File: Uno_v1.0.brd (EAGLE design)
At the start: 68.6 x 53.3 mm, 60 parts, among them CN1 POWER_JACK, CN2 47346-0001, CN3 DIGITAL10, CN4 DIGITAL8, CN5 ICSP, CN6 POWER8, CN7 ANALOG6, IC1 AMS1117-5.0, IC2 AMS1117-3.3, IC3 MCP6002T-I/SN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

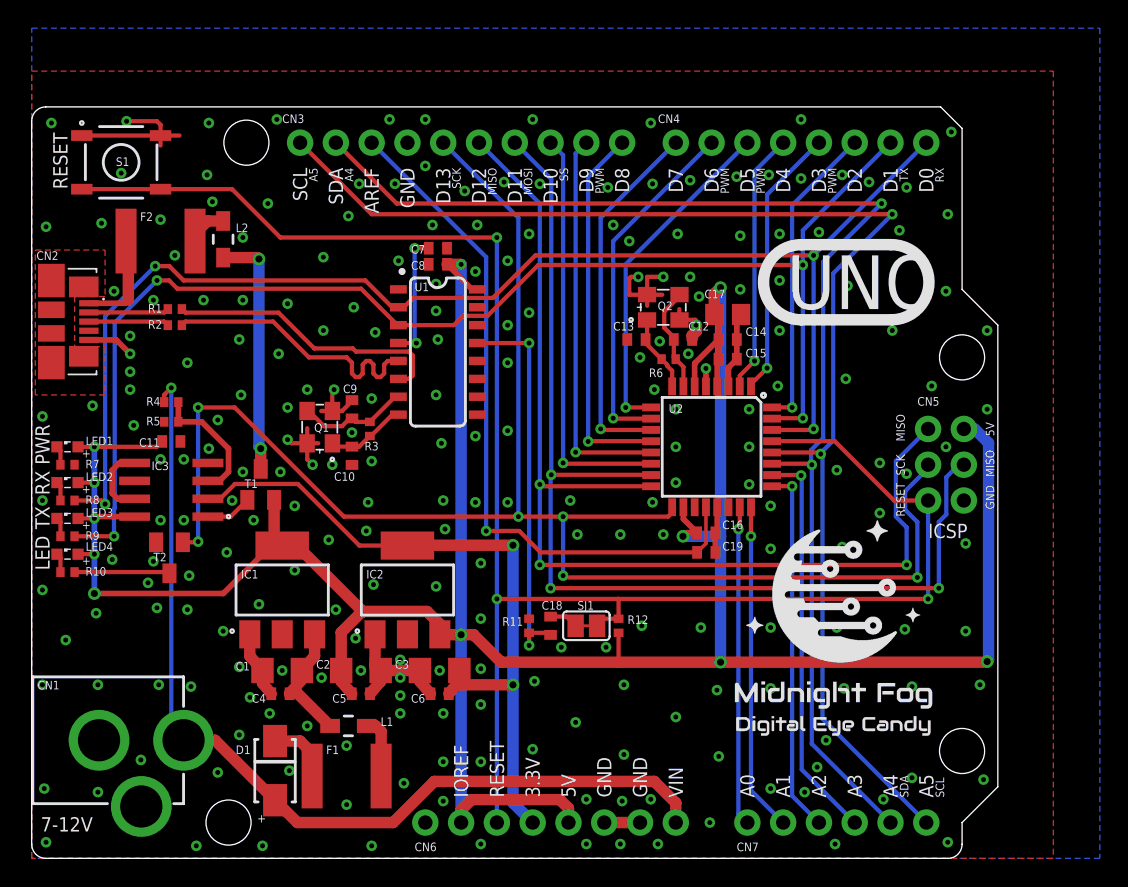
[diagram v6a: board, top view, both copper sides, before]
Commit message: Add second footprint for atmega328. Move components a little.
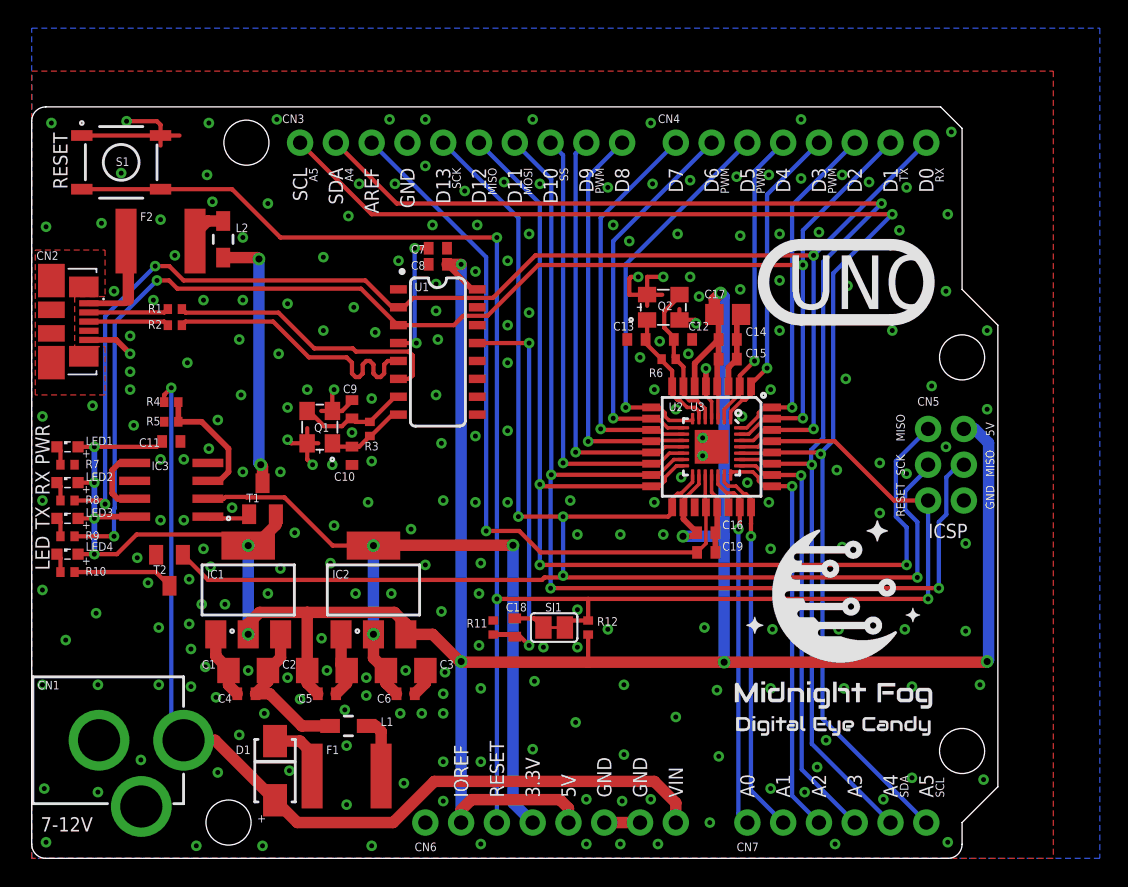
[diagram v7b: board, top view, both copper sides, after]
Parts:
- added U3: ATMEGA328P-MU, SparkFun-IC-Microcontroller:VQFN-28
- moved C18 2.54 mm to (34.3, 16.4)
- moved R11 2.54 mm to (32.8, 16.4)
- moved C1 2.41 mm to (15.4, 13.3)
- moved C2 2.41 mm to (21.0, 13.3)
- moved C3 2.41 mm to (26.5, 13.3), turned to 0 degrees
- moved C5 2.41 mm to (21.0, 11.7)
- moved C6 2.41 mm to (26.5, 11.7), turned to 0 degrees
- moved IC1 2.41 mm to (15.4, 19.1)
- moved IC2 2.41 mm to (24.3, 19.1)
- moved C4 2.41 mm to (15.2, 11.7)
- moved SJ1 2.29 mm to (37.1, 16.4)
- moved R12 2.16 mm to (39.5, 16.4)
- moved T1 1.02 mm to (16.4, 25.5)
- moved T2 0.89 mm to (9.78, 20.4)
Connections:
- net 5V: now also U3.16, U3.3
- net A0: now also U3.19
- net A1: now also U3.20
- net A2: now also U3.21
- net A3: now also U3.22
- net A4_SDA: now also U3.23
- net A5_SCL: now also U3.24
- net AREF: now also U3.17
- net D0_RX: now also U3.26
- net D10_SS: now also U3.12
- net D11_MOSI: now also U3.13
- net D12_MISO: now also U3.14
- net D13_SCK: now also U3.15
- net D1_TX: now also U3.27
- net D2: now also U3.28
- net D3_PWM: now also U3.1
- net D4: now also U3.2
- net D5_PWM: now also U3.7
- net D6_PWM: now also U3.8
- net D7: now also U3.9
- net D8: now also U3.10
- net D9_PWM: now also U3.11
- net GND: now also U3.18, U3.4, U3.PAD
- net MCU_OSC_IN: now also U3.5
- net MCU_OSC_OUT: now also U3.6
- net RESET: now also U3.25
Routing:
- net 5V: track 219.2 -> 225.0 mm, vias 11 -> 12
- net D13_SCK: track 115.2 -> 109.5 mm, vias 6 -> 4
- net 3.3V: track 50.8 -> 55.4 mm, vias 2 -> 3
- net A2: track 26.1 -> 29.8 mm
- net D5_PWM: track 24.2 -> 27.8 mm
- net MCU_OSC_OUT: track 5.54 -> 9.05 mm
- net A1: track 23.3 -> 26.8 mm
- net MCU_OSC_IN: track 7.53 -> 10.8 mm
- net A0: track 22.7 -> 25.9 mm
- net D12_MISO: track 76.7 -> 79.7 mm
- net D3_PWM: track 19.3 -> 22.3 mm
- net D2: track 22.1 -> 25.1 mm
- net D11_MOSI: track 77.1 -> 79.8 mm
- net D4: track 18.6 -> 21.3 mm
- net D1_TX: track 95.5 -> 98.2 mm
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
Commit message: Rotated CH340G 180 degrees. Moved stuff around a little.
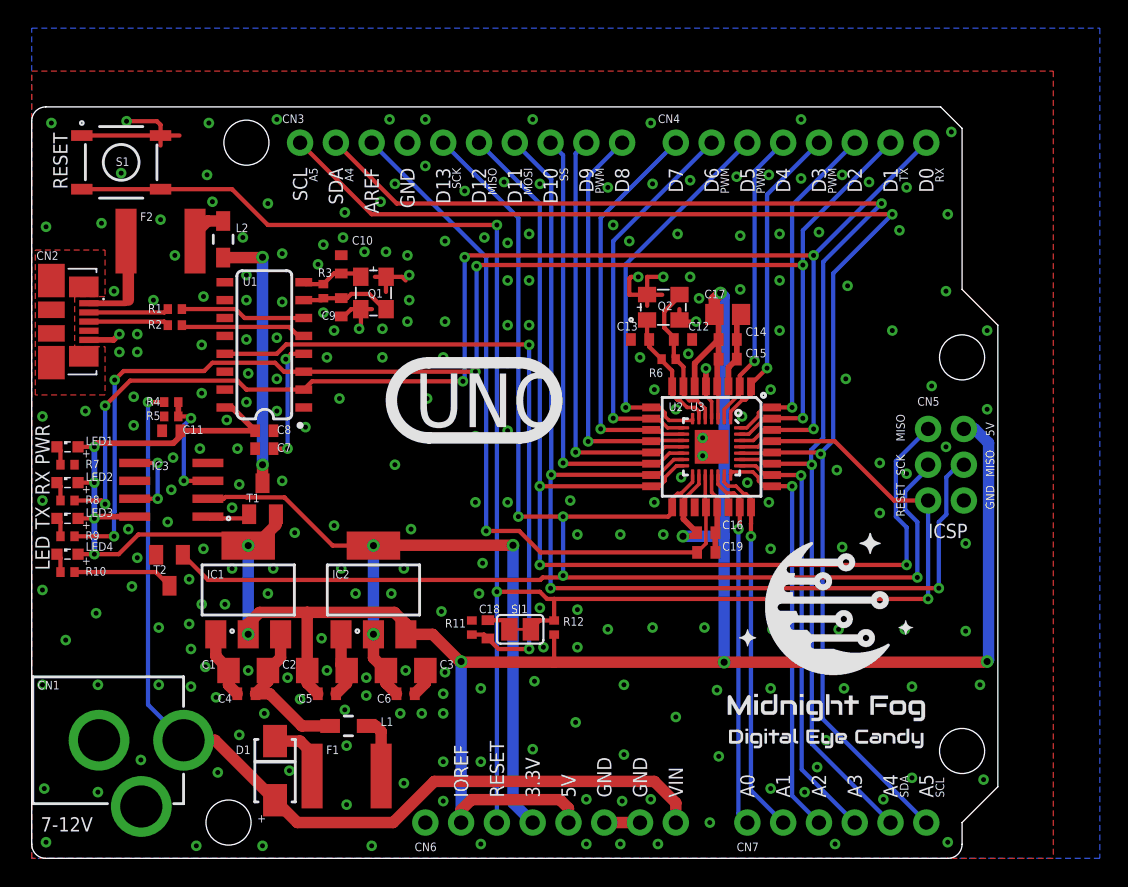
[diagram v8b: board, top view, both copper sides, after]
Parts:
- moved C7 18.8 mm to (16.5, 29.1), turned to 0 degrees
- moved C8 17.1 mm to (16.5, 30.4), turned to 0 degrees
- moved C10 13.6 mm to (22.0, 42.2), turned to 270 degrees
- moved U1 12.3 mm to (16.5, 36.4), turned to 90 degrees
- moved R3 10.3 mm to (20.7, 40.3), turned to 270 degrees
- moved Q1 10.3 mm to (24.3, 40.1), turned to 270 degrees
- moved C9 7.28 mm to (22.0, 39.1), turned to 90 degrees
- moved SJ1 2.42 mm to (34.7, 16.3)
- moved R12 2.41 mm to (37.1, 16.4)
- moved C18 1.91 mm to (32.4, 16.3)
- moved R11 1.52 mm to (31.2, 16.4)
- moved LOGO1 1.02 mm to (48.4, 7.37)
- moved C11 0.76 mm to (9.91, 30.4), turned to 180 degrees
- moved R5 0.38 mm to (9.91, 31.4)
- moved C13 0.25 mm to (43.2, 36.8)
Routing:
- net 5V: track 225.0 -> 202.9 mm, vias 12 -> 11
- net USB_DTR: track 29.6 -> 48.0 mm
- net USB_D_M: track 20.3 -> 8.91 mm
- net USB_D_P: track 20.1 -> 8.97 mm
- net GND: track 62.3 -> 59.0 mm, vias 245 -> 254
- net USB_OSC_IN: track 8.00 -> 6.48 mm
- net USB_OSC_OUT: track 5.72 -> 4.51 mm
- net N$12: track 9.13 -> 8.33 mm, vias 0 -> 2
- net N$1: track 5.20 -> 5.81 mm, vias 0 -> 2
- net D0_RX: track 99.3 -> 98.8 mm, vias 4 -> 6
- net D1_TX: track 98.2 -> 98.1 mm, vias 4 -> 6
